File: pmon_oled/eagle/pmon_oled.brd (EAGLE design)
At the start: 60 x 60 mm, 37 parts, among them J1 USB, J2 USB, J4 PINHD-1X3, J5 PINHD-2X3, Q1 16Mhz, U1 LTC2943, U2 FT232RL, U3 LT1764AEQ, U4 ATMEGA328TQFP32

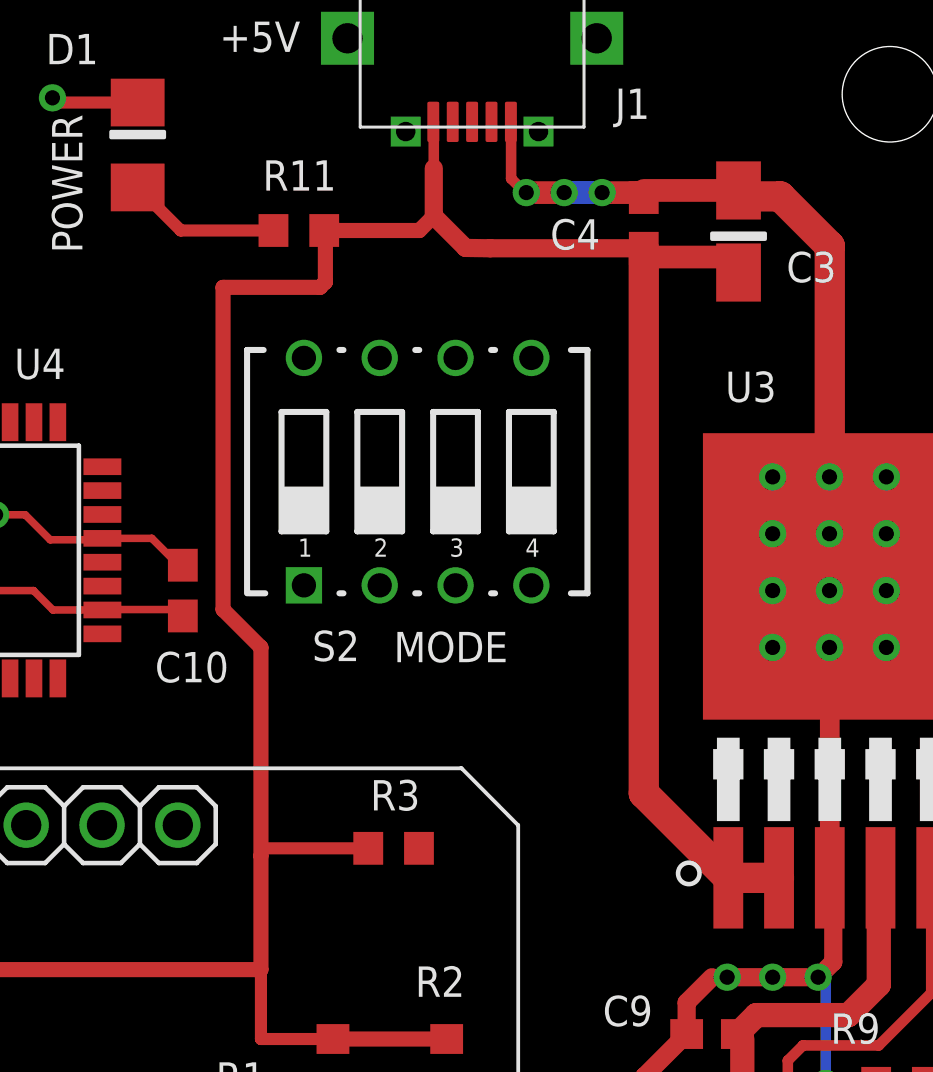
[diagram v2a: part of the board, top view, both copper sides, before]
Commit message: Tweaks criticla nets to improve auto rounting. Should be ready for final auto routing.
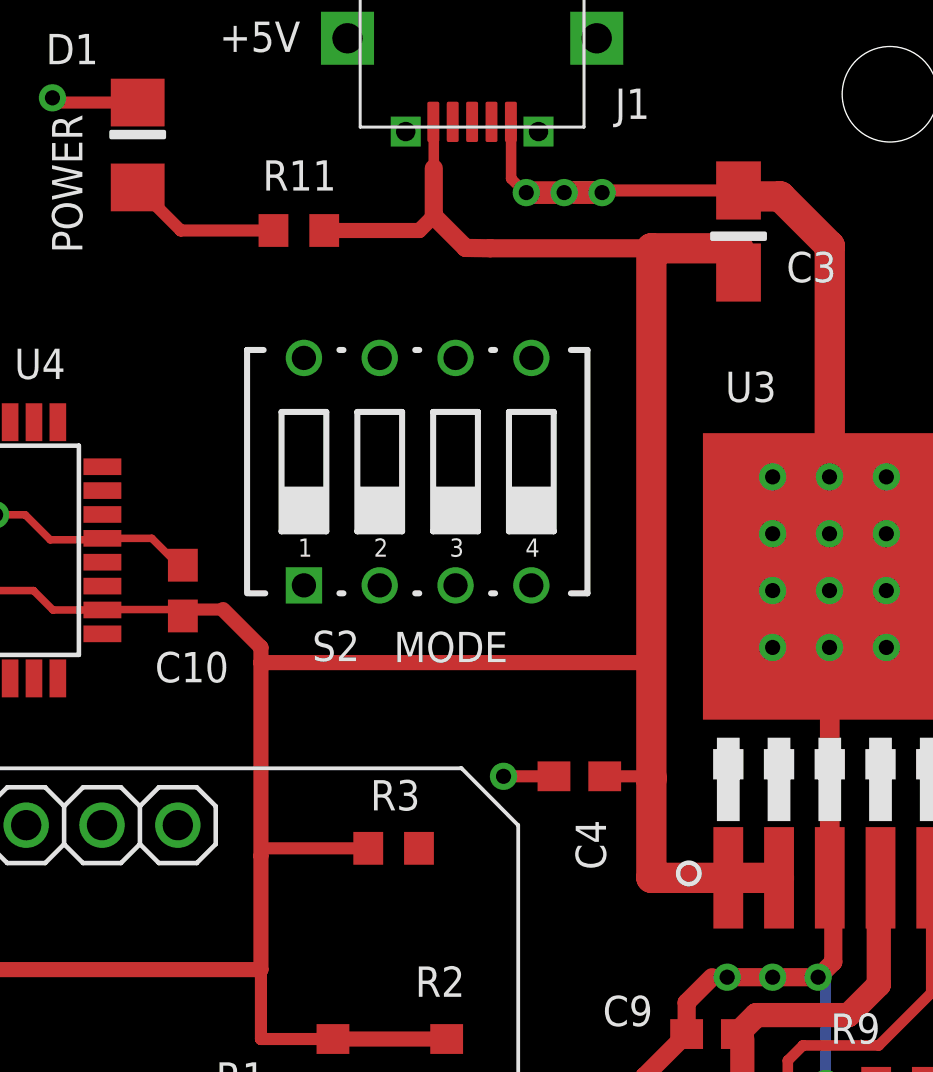
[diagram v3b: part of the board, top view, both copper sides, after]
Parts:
- moved C4 18.7 mm to (45.6, 33.1), turned to 180 degrees
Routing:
- net +5V: track 150.0 -> 154.9 mm
- net GND: track 115.2 -> 117.9 mm, vias 29 -> 30
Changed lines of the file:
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@@
 <attribute name="NAME" x="52.531409375" y="49.70061875" size="1.016" layer="25" font="vector" ratio="10"/>
 </element>
-<element name="C4" library="pmon_oled" package="C0603" value="0.1uF" x="47.752" y="51.689" smashed="yes" rot="R90">
-<attribute name="NAME" x="44.617015625" y="50.795365625" size="1.016" layer="25" font="vector" ratio="10"/>
+<element name="C4" library="pmon_oled" package="C0603" value="0.1uF" x="45.593" y="33.147" smashed="yes" rot="R180">
+<attribute name="NAME" x="46.486634375" y="30.012015625" size="1.016" layer="25" font="vector" ratio="10" rot="R90"/>
 </element>
 <element name="C9" library="pmon_oled" package="C0603" value="0.1uF" x="50.038" y="24.511" smashed="yes" rot="R180">
@@
 <wire x1="43.3" y1="55.075" x2="43.307" y2="55.075" width="0.3556" layer="1"/>
 <wire x1="43.307" y1="55.075" x2="43.307" y2="53.174" width="0.3556" layer="1"/>
-<wire x1="47.752" y1="52.539" x2="47.752" y2="52.777" width="0.3556" layer="1"/>
-<wire x1="47.752" y1="52.777" x2="50.927" y2="52.777" width="0.762" layer="1"/>
 <wire x1="50.927" y1="52.777" x2="50.927" y2="52.705" width="0.3556" layer="1"/>
 <wire x1="53.984" y1="29.745" x2="54.102" y2="29.627" width="0.3556" layer="1"/>
@@
 <via x="52.07" y="41.275" extent="1-16" drill="0.508"/>
 <via x="53.975" y="41.275" extent="1-16" drill="0.508"/>
-<wire x1="47.752" y1="52.539" x2="47.586" y2="52.705" width="0.762" layer="1"/>
-<wire x1="47.586" y1="52.705" x2="46.355" y2="52.705" width="0.762" layer="1"/>
 <via x="46.355" y="52.705" extent="1-16" drill="0.508"/>
 <wire x1="46.355" y1="52.705" x2="45.085" y2="52.705" width="0.762" layer="16"/>
@@
 <via x="27.94" y="55.88" extent="1-16" drill="0.508"/>
 <contactref element="S1" pad="A"/>
-<wire x1="53.975" y1="43.18" x2="55.88" y2="43.18" width="0" layer="19" extent="1-1"/>
-<wire x1="55.88" y1="41.275" x2="55.88" y2="43.18" width="0" layer="19" extent="1-1"/>
-<wire x1="52.07" y1="43.18" x2="53.975" y2="43.18" width="0" layer="19" extent="1-1"/>
-<wire x1="55.88" y1="39.37" x2="55.88" y2="41.275" width="0" layer="19" extent="1-1"/>
-<wire x1="53.975" y1="41.275" x2="53.975" y2="43.18" width="0" layer="19" extent="1-1"/>
-<wire x1="53.984" y1="39.845" x2="53.975" y2="41.275" width="0" layer="19" extent="1-1"/>
-<wire x1="53.975" y1="39.37" x2="53.984" y2="39.845" width="0" layer="19" extent="1-1"/>
-<wire x1="55.88" y1="37.465" x2="55.88" y2="39.37" width="0" layer="19" extent="1-1"/>
-<wire x1="52.07" y1="41.275" x2="52.07" y2="43.18" width="0" layer="19" extent="1-1"/>
-<wire x1="52.07" y1="39.37" x2="53.975" y2="39.37" width="0" layer="19" extent="1-1"/>
-<wire x1="53.975" y1="37.465" x2="53.975" y2="39.37" width="0" layer="19" extent="1-1"/>
-<wire x1="52.07" y1="37.465" x2="52.07" y2="39.37" width="0" layer="19" extent="1-1"/>
-<wire x1="46.394" y1="15.748" x2="47.774" y2="21.717" width="0" layer="19" extent="1-1"/>
-<wire x1="45.724" y1="14.558" x2="46.228" y2="14.562" width="0" layer="19" extent="1-1"/>
-<wire x1="46.435" y1="5.475" x2="46.224" y2="11.858" width="0" layer="19" extent="1-1"/>
-<wire x1="43.985" y1="39.545" x2="52.07" y2="39.37" width="0" layer="19" extent="1-1"/>
-<wire x1="41.445" y1="39.545" x2="43.985" y2="39.545" width="0" layer="19" extent="1-1"/>
-<wire x1="38.905" y1="39.545" x2="41.445" y2="39.545" width="0" layer="19" extent="1-1"/>
-<wire x1="36.365" y1="39.545" x2="38.905" y2="39.545" width="0" layer="19" extent="1-1"/>
-<wire x1="32.3088" y1="40.22" x2="36.365" y2="39.545" width="0" layer="19" extent="1-1"/>
-<wire x1="21.0274" y1="40.32" x2="21.0274" y2="41.92" width="0" layer="19" extent="1-1"/>
-<wire x1="19.44" y1="31.51" x2="19.4818" y2="31.5468" width="0" layer="19" extent="16-16"/>
-<wire x1="14.605" y1="44.87" x2="17.995" y2="41.91" width="0" layer="19" extent="1-1"/>
-<wire x1="7.39" y1="48.346" x2="9.34" y2="48.346" width="0" layer="19" extent="1-1"/>
-<wire x1="12.065" y1="54.19" x2="9.34" y2="48.346" width="0" layer="19" extent="1-1"/>
-<wire x1="19.3" y1="55.075" x2="12.065" y2="54.19" width="0" layer="19" extent="1-1"/>
-<wire x1="27.94" y1="55.88" x2="19.3294" y2="55.0456" width="0" layer="19" extent="1-1"/>
-<wire x1="2.855" y1="29.21" x2="6.74" y2="41.034" width="0" layer="19" extent="1-1"/>
-<wire x1="2.0477375" y1="20.24769375" x2="2.855" y2="29.21" width="0" layer="19" extent="1-1"/>
+<wire x1="45.085" y1="52.705" x2="46.355" y2="52.705" width="0.762" layer="1"/>
+<wire x1="50.927" y1="52.777" x2="46.355" y2="52.777" width="0.4064" layer="1"/>
+<wire x1="46.355" y1="52.777" x2="46.355" y2="52.705" width="0.4064" layer="1"/>
+<wire x1="44.743" y1="33.147" x2="43.053" y2="33.147" width="0.4064" layer="1"/>
+<via x="43.053" y="33.147" extent="1-16" drill="0.508"/>
+<wire x1="46.228" y1="14.562" x2="45.724" y2="14.558" width="0" layer="19" extent="1-1"/>
+<wire x1="47.774" y1="21.717" x2="46.394" y2="15.748" width="0" layer="19" extent="1-1"/>
 </signal>
 <signal name="+5V">
@@
 <wire x1="40.7162" y1="51.9176" x2="41.783" y2="50.8508" width="0.6096" layer="1"/>
 <wire x1="41.783" y1="50.8508" x2="42.605" y2="50.839" width="0.6096" layer="1"/>
-<wire x1="47.498" y1="50.839" x2="47.752" y2="50.839" width="0.3556" layer="1"/>
-<wire x1="47.752" y1="50.839" x2="47.752" y2="50.546" width="0.3556" layer="1"/>
-<wire x1="47.752" y1="50.546" x2="50.8" y2="50.546" width="0.762" layer="1"/>
-<wire x1="50.8" y1="50.546" x2="50.8" y2="50.027" width="0.3556" layer="1"/>
-<wire x1="50.8" y1="50.027" x2="50.927" y2="50.027" width="0.3556" layer="1"/>
-<wire x1="42.605" y1="50.839" x2="47.752" y2="50.839" width="0.6096" layer="1"/>
 <wire x1="50.584" y1="29.745" x2="52.284" y2="29.745" width="1.016" layer="1"/>
-<wire x1="50.584" y1="29.745" x2="47.752" y2="32.577" width="1.016" layer="1"/>
-<wire x1="47.752" y1="32.577" x2="47.752" y2="50.839" width="1.016" layer="1"/>
 <wire x1="21.0274" y1="39.52" x2="21.1774" y2="39.37" width="0.254" layer="1"/>
 <wire x1="21.1774" y1="39.37" x2="23.495" y2="39.37" width="0.254" layer="1"/>
@@
 <wire x1="40.2336" y1="51.435" x2="37.045" y2="51.435" width="0.508" layer="1"/>
 <wire x1="37.045" y1="51.435" x2="37.084" y2="51.396" width="0.508" layer="1"/>
-<wire x1="37.084" y1="51.396" x2="37.084" y2="49.7078" width="0.508" layer="1"/>
-<wire x1="37.084" y1="49.7078" x2="36.9062" y2="49.53" width="0.508" layer="1"/>
-<wire x1="36.9062" y1="49.53" x2="33.655" y2="49.53" width="0.508" layer="1"/>
-<wire x1="33.655" y1="49.53" x2="33.655" y2="38.735" width="0.508" layer="1"/>
 <wire x1="33.655" y1="38.735" x2="34.925" y2="37.465" width="0.508" layer="1"/>
-<wire x1="34.925" y1="37.465" x2="34.925" y2="30.48" width="0.508" layer="1"/>
+<wire x1="34.925" y1="37.465" x2="34.925" y2="36.957" width="0.508" layer="1"/>
+<wire x1="34.925" y1="36.957" x2="34.925" y2="30.48" width="0.508" layer="1"/>
 <wire x1="34.925" y1="30.48" x2="34.925" y2="26.67" width="0.508" layer="1"/>
 <wire x1="37.123" y1="24.345" x2="37.338" y2="24.345" width="0.508" layer="1"/>
@@
 <wire x1="37.123" y1="24.345" x2="34.925" y2="24.345" width="0.4064" layer="1"/>
 <wire x1="34.925" y1="24.345" x2="34.925" y2="26.67" width="0.4064" layer="1"/>
-<wire x1="33.655" y1="38.735" x2="32.385" y2="38.735" width="0" layer="19" extent="1-1"/>
+<wire x1="32.385" y1="38.735" x2="33.655" y2="38.735" width="0.4064" layer="1"/>
+<wire x1="34.925" y1="36.957" x2="47.879" y2="36.957" width="0.508" layer="1"/>
+<wire x1="42.605" y1="50.839" x2="48.006" y2="50.839" width="0.6096" layer="1"/>
+<wire x1="48.006" y1="50.839" x2="50.927" y2="50.839" width="1.016" layer="1"/>
+<wire x1="50.927" y1="50.839" x2="50.927" y2="50.027" width="0.4064" layer="1"/>
+<wire x1="50.584" y1="29.745" x2="48.006" y2="29.745" width="1.016" layer="1"/>
+<wire x1="48.006" y1="29.745" x2="48.006" y2="33.02" width="1.016" layer="1"/>
+<wire x1="48.006" y1="33.02" x2="48.006" y2="33.147" width="1.016" layer="1"/>
+<wire x1="48.006" y1="33.147" x2="48.006" y2="50.839" width="1.016" layer="1"/>
+<wire x1="46.443" y1="33.147" x2="48.006" y2="33.147" width="0.4064" layer="1"/>
+<wire x1="47.879" y1="36.957" x2="48.006" y2="36.957" width="0.4064" layer="1"/>
+<wire x1="48.006" y1="36.957" x2="48.006" y2="33.147" width="0.4064" layer="1"/>
 </signal>
 <signal name="RESET">
@@
 <contactref element="U1" pad="4"/>
 <contactref element="U4" pad="28"/>
-<wire x1="40.22" y1="30.734" x2="25.72" y2="45.0126" width="0" layer="19" extent="1-1"/>
 <wire x1="45.224" y1="14.558" x2="40.22" y2="30.734" width="0" layer="19" extent="1-1"/>
+<wire x1="25.72" y1="45.0126" x2="40.22" y2="30.734" width="0" layer="19" extent="1-1"/>
 </signal>
 <signal name="I2C-DATA">
